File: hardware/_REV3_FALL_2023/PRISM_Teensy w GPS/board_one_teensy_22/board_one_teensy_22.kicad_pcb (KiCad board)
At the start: 2 copper layers, 61 x 88.9 mm, 26 parts, among them J1 Micro_SD_Card_Det_Hirose_DM3AT, J3 3387, U1 Teensy4.0, U2 GPS-14414, U3 3966, U4 RFM69HCW_Breakout, U5 SFN-1407PA7.6

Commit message: Final PRISM GPS Board
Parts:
- moved C2 5.63 mm to (146.5, 90.7)
- moved D3 5.63 mm to (151.0, 90.8)
- moved D5 5.63 mm to (158.6, 90.8)
- moved C1 4.44 mm to (139.7, 90.7)
- moved R4 4.44 mm to (141.9, 91.4)
- moved R5 4.44 mm to (141.9, 89.9)
- moved C3 1.51 mm to (131.8, 90.5)
- moved R1 1.51 mm to (132.5, 84.6)
- moved R3 1.51 mm to (132.5, 86.1)
- moved R2 1.51 mm to (132.6, 93.8)
- moved U3 1.20 mm to (126.3, 123.7)
- moved J3 0.32 mm to (152.4, 122.9)
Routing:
- net GND: track 0.00 -> 277.3 mm, vias 0 -> 4
- net /5V: track 0.00 -> 148.4 mm
- net /3.3V: track 0.00 -> 122.6 mm, vias 0 -> 2
- net /ARM: track 0.00 -> 111.7 mm, vias 0 -> 1
- net /CONT 1: track 0.00 -> 108.3 mm, vias 0 -> 2
- net /SDA: track 0.00 -> 105.0 mm, vias 0 -> 5
- net /CONT 2: track 0.00 -> 104.7 mm, vias 0 -> 2
- net /PYRO 1: track 0.00 -> 101.0 mm
- net /PYRO 2: track 0.00 -> 100.0 mm, vias 0 -> 2
- net /SCL: track 0.00 -> 89.9 mm, vias 0 -> 4
- net /SD_SCK: track 0.00 -> 65.8 mm, vias 0 -> 2
- net /SD_DETECT: track 0.00 -> 58.2 mm
- net /VBAT: track 0.00 -> 52.9 mm
- net /EN: track 0.00 -> 49.3 mm, vias 0 -> 2
- net /MOSI: track 0.00 -> 48.1 mm, vias 0 -> 5
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
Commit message: Finished stepper implementation
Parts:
- added R6: 1k, Resistor_SMD:R_0603_1608Metric_Pad0.98x0.95mm_HandSolder, F.Cu at (125.7, 112.9)
- C1, C2, C3: footprint Capacitor_SMD:C_0603_1608Metric -> Capacitor_SMD:C_0603_1608Metric_Pad1.08x0.95mm_HandSolder
- R1, R2, R3, R4, R5: footprint Resistor_SMD:R_0603_1608Metric -> Resistor_SMD:R_0603_1608Metric_Pad0.98x0.95mm_HandSolder
- Stepper1: value Conn_01x05_Socket -> Conn_01x03_Socket; footprint Connector_PinHeader_2.54mm:PinHeader_1x05_P2.54mm_Vertical -> Connector_PinHeader_2.54mm:PinHeader_1x03_P2.54mm_Vertical
- moved Stepper1 4.97 mm to (111.3, 111.8)
- moved Power1 4.74 mm to (111.3, 102.9)
- moved C1 0.25 mm to (139.4, 90.7)
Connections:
- net /RX 4 renamed /UART
- Stepper1 pad 2: /TX 4 -> /DIR
- Stepper1 pad 3: /EN -> /STEP
- U1 pad 17: /TX 4 -> Net-(R6-Pad1)
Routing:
- net /EN: track 49.3 -> 0.00 mm, vias 2 -> 0
- net /TX 4: track 32.9 -> 0.00 mm
- net Net-(R6-Pad1): track 0.00 -> 16.5 mm
- net /STEP: track 46.3 -> 35.7 mm
- net /VBAT: track 52.9 -> 58.4 mm
- net /5V: track 148.4 -> 153.2 mm
- net /UART: track 30.9 -> 28.8 mm
- net GND: track 277.3 -> 279.3 mm
- net /SD_SCK: track 65.8 -> 66.7 mm
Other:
- board text added: "ST DR UX"
- board text removed: "ST DR EN TX RX"

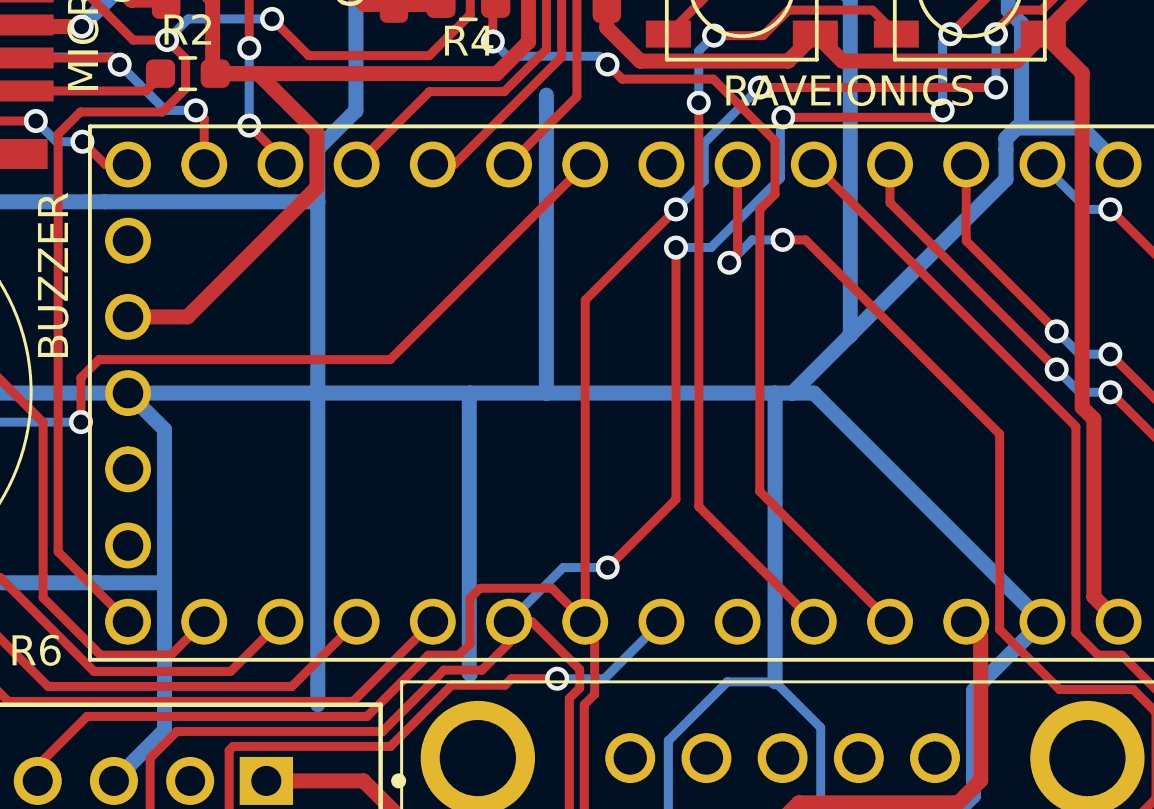
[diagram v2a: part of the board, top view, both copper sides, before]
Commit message: Fix problem with 3V3 plane
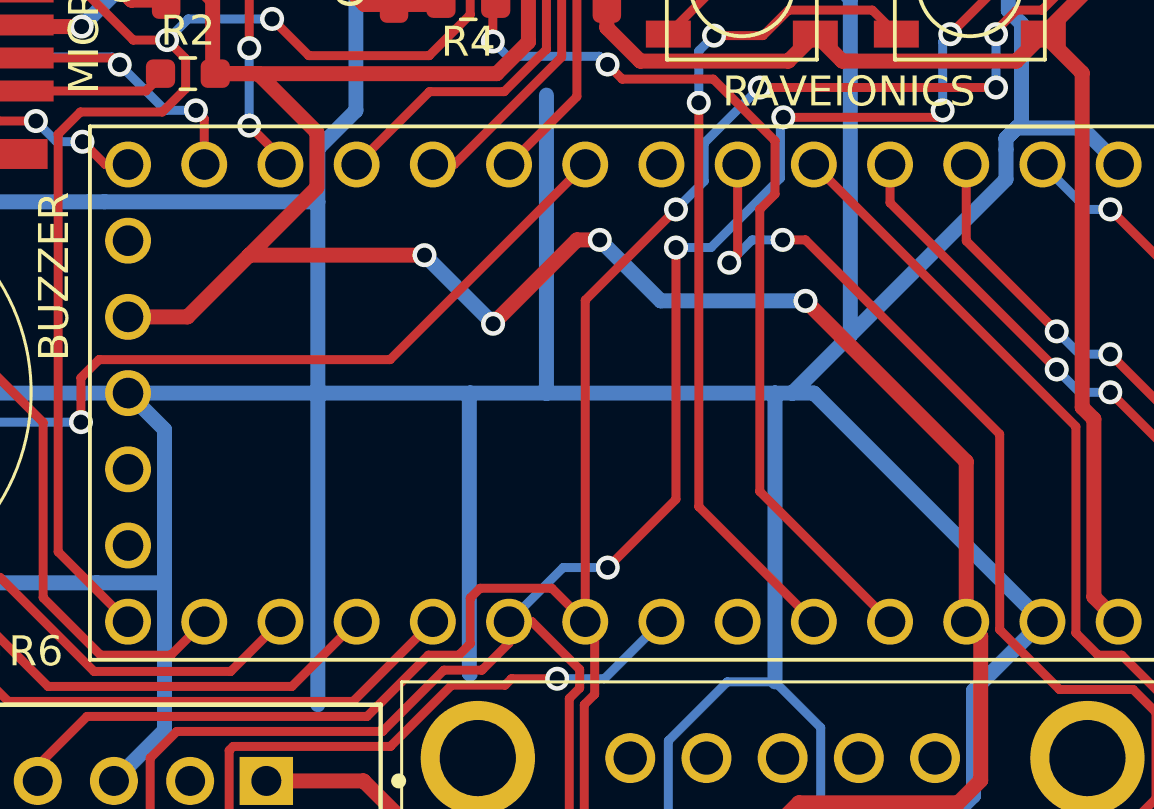
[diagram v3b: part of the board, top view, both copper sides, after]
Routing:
- net /3.3V: track 122.9 -> 157.3 mm, vias 2 -> 6
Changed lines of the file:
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@@
   (via (at 134.62 92.9225) (size 0.8) (drill 0.5) (layers "F.Cu" "B.Cu") (net 10))
   (segment (start 134.62 95.504) (end 134.62 92.9225) (width 0.3) (layer "B.Cu") (net 10))
+  (segment (start 158.52 106.704) (end 153.162 101.346) (width 0.5) (layer "F.Cu") (net 16))
   (segment (start 143.598 86.693) (end 143.598 88.810296) (width 0.5) (layer "F.Cu") (net 16))
   (segment (start 145.034 129.032) (end 144.78 129.286) (width 0.5) (layer "F.Cu") (net 16))
   (segment (start 127.1 89.95) (end 131.672 89.95) (width 0.5) (layer "F.Cu") (net 16))
   (segment (start 133.35 86.868) (end 133.35 86.072) (width 0.5) (layer "F.Cu") (net 16))
+  (segment (start 146.304 99.314) (end 145.542 99.314) (width 0.5) (layer "F.Cu") (net 16))
   (segment (start 159.0025 117.329617) (end 159.0025 112.5225) (width 0.5) (layer "F.Cu") (net 16))
   (segment (start 138.43 117.348) (end 135.19 117.348) (width 0.5) (layer "F.Cu") (net 16))
+  (segment (start 134.62 99.822) (end 136.875 97.567) (width 0.5) (layer "F.Cu") (net 16))
   (segment (start 131.85 89.772) (end 131.85 88.368) (width 0.5) (layer "F.Cu") (net 16))
   (segment (start 159.0025 112.5225) (end 158.52 112.04) (width 0.5) (layer "F.Cu") (net 16))
   (segment (start 158.254178 118.077939) (end 159.0025 117.329617) (width 0.5) (layer "F.Cu") (net 16))
+  (segment (start 140.462 99.822) (end 134.62 99.822) (width 0.5) (layer "F.Cu") (net 16))
   (segment (start 136.365 79.46) (end 143.598 86.693) (width 0.5) (layer "F.Cu") (net 16))
   (segment (start 131.672 89.95) (end 131.85 89.772) (width 0.5) (layer "F.Cu") (net 16))
   (segment (start 134.92 93.772) (end 133.4 93.772) (width 0.5) (layer "F.Cu") (net 16))
+  (segment (start 132.562 101.88) (end 134.62 99.822) (width 0.5) (layer "F.Cu") (net 16))
   (segment (start 145.034 123.952) (end 138.43 117.348) (width 0.5) (layer "F.Cu") (net 16))
   (segment (start 142.869472 93.772) (end 133.4 93.772) (width 0.5) (layer "F.Cu") (net 16))
@@
   (segment (start 136.875 97.567) (end 136.875 95.727) (width 0.5) (layer "F.Cu") (net 16))
   (segment (start 152.940061 118.077939) (end 158.254178 118.077939) (width 0.5) (layer "F.Cu") (net 16))
-  (segment (start 132.562 101.88) (end 136.875 97.567) (width 0.5) (layer "F.Cu") (net 16))
   (segment (start 130.58 101.88) (end 132.562 101.88) (width 0.5) (layer "F.Cu") (net 16))
   (segment (start 131.85 88.368) (end 133.35 86.868) (width 0.5) (layer "F.Cu") (net 16))
   (segment (start 143.926 92.715472) (end 142.869472 93.772) (width 0.5) (layer "F.Cu") (net 16))
+  (segment (start 158.52 112.04) (end 158.52 106.704) (width 0.5) (layer "F.Cu") (net 16))
   (segment (start 133.35 86.072) (end 133.35 84.582) (width 0.5) (layer "F.Cu") (net 16))
   (segment (start 163.2935 71.85) (end 158.441 71.85) (width 0.5) (layer "F.Cu") (net 16))
+  (segment (start 145.542 99.314) (end 142.748 102.108) (width 0.5) (layer "F.Cu") (net 16))
   (segment (start 158.441 71.85) (end 143.598 86.693) (width 0.5) (layer "F.Cu") (net 16))
   (segment (start 136.875 95.727) (end 134.92 93.772) (width 0.5) (layer "F.Cu") (net 16))
@@
   (segment (start 143.598 88.810296) (end 143.926 89.138296) (width 0.5) (layer "F.Cu") (net 16))
   (segment (start 133.4 93.772) (end 133.4 91.322) (width 0.5) (layer "F.Cu") (net 16))
+  (via (at 142.748 102.108) (size 0.8) (drill 0.5) (layers "F.Cu" "B.Cu") (net 16))
+  (via (at 140.462 99.822) (size 0.8) (drill 0.5) (layers "F.Cu" "B.Cu") (net 16))
+  (via (at 153.162 101.346) (size 0.8) (drill 0.5) (layers "F.Cu" "B.Cu") (net 16))
   (via (at 147.066 123.952) (size 0.8) (drill 0.5) (layers "F.Cu" "B.Cu") (net 16))
+  (via (at 146.304 99.314) (size 0.8) (drill 0.5) (layers "F.Cu" "B.Cu") (net 16))
   (via (at 145.034 123.952) (size 0.8) (drill 0.5) (layers "F.Cu" "B.Cu") (net 16))
   (segment (start 145.034 123.952) (end 147.066 123.952) (width 0.5) (layer "B.Cu") (net 16))
+  (segment (start 153.162 101.346) (end 148.336 101.346) (width 0.5) (layer "B.Cu") (net 16))
+  (segment (start 142.748 102.108) (end 140.462 99.822) (width 0.5) (layer "B.Cu") (net 16))
+  (segment (start 148.336 101.346) (end 146.304 99.314) (width 0.5) (layer "B.Cu") (net 16))
   (segment (start 113.25 84.108) (end 116.332 81.026) (width 0.5) (layer "F.Cu") (net 19))
   (segment (start 141.072 91.466) (end 141.098 91.44) (width 0.5) (layer "F.Cu") (net 19))
